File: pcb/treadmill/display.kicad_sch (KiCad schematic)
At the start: 34 parts, among them J1 KEY, J2 TO_MOTOR_BOARD, J3 PRG2, J4 PRG, J5 EXT_SERIAL?, Q1 "J3" SS9013 NPN, Q2 "2T1" SS9012 PNP, U1 LM78M05_TO252, U2 PL51WT020, U3 STM8S005K6T6C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

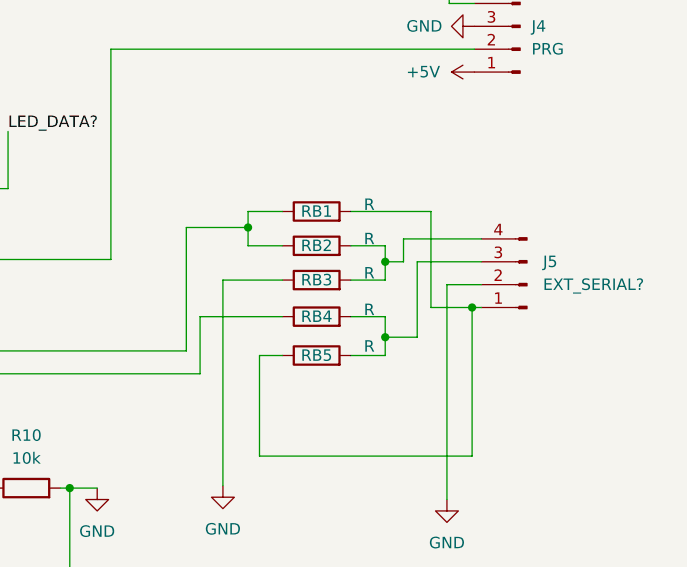
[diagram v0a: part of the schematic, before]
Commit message: Figuring out more connections from the control board, mostly
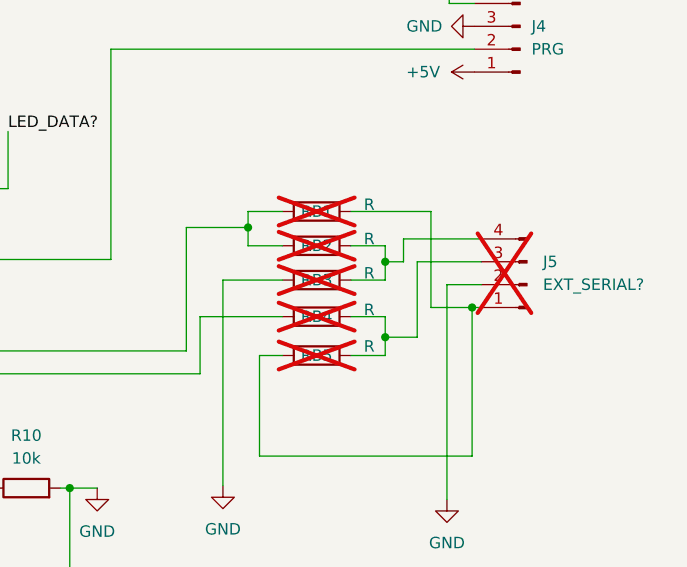
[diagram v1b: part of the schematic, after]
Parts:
- J5, RB1, RB2, RB3, RB4, RB5: now not fitted
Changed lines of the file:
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@@
 		(in_bom yes)
 		(on_board yes)
-		(dnp no)
+		(dnp yes)
 		(property "Reference" "RB1"
 			(at 230.124 86.614 90)
@@
 		(in_bom yes)
 		(on_board yes)
-		(dnp no)
+		(dnp yes)
 		(property "Reference" "RB5"
 			(at 230.124 102.616 90)
@@
 		(in_bom yes)
 		(on_board yes)
-		(dnp no)
+		(dnp yes)
 		(property "Reference" "RB2"
 			(at 230.124 90.424 90)
@@
 		(in_bom yes)
 		(on_board yes)
-		(dnp no)
+		(dnp yes)
 		(fields_autoplaced yes)
 		(property "Reference" "J5"
@@
 		(in_bom yes)
 		(on_board yes)
-		(dnp no)
+		(dnp yes)
 		(property "Reference" "RB4"
 			(at 230.124 98.298 90)
@@
 		(in_bom yes)
 		(on_board yes)
-		(dnp no)
+		(dnp yes)
 		(property "Reference" "RB3"
 			(at 230.124 94.234 90)
